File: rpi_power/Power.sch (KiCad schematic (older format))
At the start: 27 parts, among them U1 TPS54625

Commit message: Updated some footprints.
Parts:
- C10, C11: footprint Capacitor_Tantalum_SMD:CP_EIA-3216-10_Kemet-I_Pad1.58x1.35mm_HandSolder -> Capacitors:Tantalum_SMD_3216_KEMET_T491_HandSolder
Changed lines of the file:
@@
 F 0 "C10" H 9568 3146 50  0000 L CNN
 F 1 "22uF/6.3V" H 9568 3055 50  0000 L CNN
-F 2 "Capacitor_Tantalum_SMD:CP_EIA-3216-10_Kemet-I_Pad1.58x1.35mm_HandSolder" H 9488 2950 50  0001 C CNN
+F 2 "Capacitors:Tantalum_SMD_3216_KEMET_T491_HandSolder" H 9488 2950 50  0001 C CNN
 F 3 "~" H 9450 3100 50  0001 C CNN
 F 4 "2321204" H 150 -300 50  0001 C CNN "Farnell"
@@
 F 0 "C11" H 10118 2646 50  0000 L CNN
 F 1 "22uF/6.3V" H 10118 2555 50  0000 L CNN
-F 2 "Capacitor_Tantalum_SMD:CP_EIA-3216-10_Kemet-I_Pad1.58x1.35mm_HandSolder" H 10038 2450 50  0001 C CNN
+F 2 "Capacitors:Tantalum_SMD_3216_KEMET_T491_HandSolder" H 10038 2450 50  0001 C CNN
 F 3 "~" H 10000 2600 50  0001 C CNN
 F 4 "2321204" H 700 -800 50  0001 C CNN "Farnell"

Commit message: Routing done, pending review.
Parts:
- U1: footprint TexasInstruments:HTSSOP-14-PWP -> TexasInstruments:HTSSOP-14-PWP_Handsolder
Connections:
- wire segments 106 -> 92
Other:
- moved on the sheet: C1, C10, C11, C2, C3, C4, C5, C6, C7, C8, C9, D1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

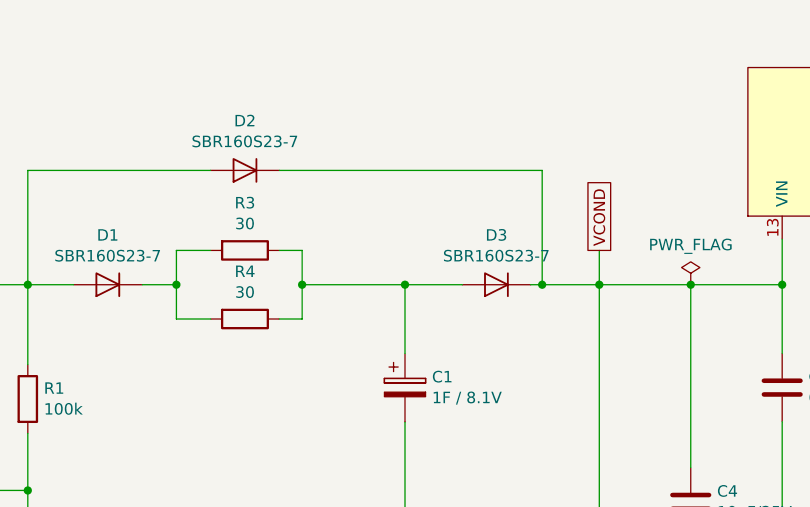
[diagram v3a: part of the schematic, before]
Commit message: Differentiated VCOND and BATT+. Routing done.
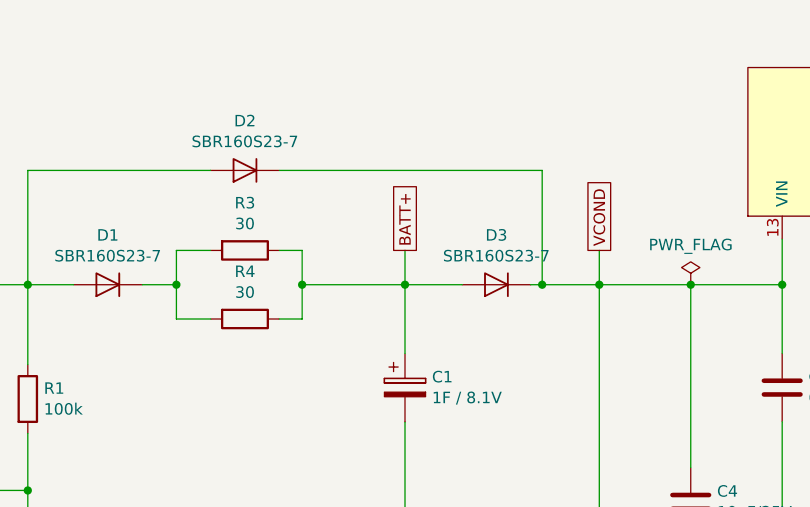
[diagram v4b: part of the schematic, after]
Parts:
- MH1, MH2, MH3, MH4: footprint MountingHole:MountingHole_3.2mm_M3_DIN965 -> Pads:MountingHole_M3-5.8_Pad_Via
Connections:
- net BATT+: now reaches C1.1, D3.2 (A), R3.1, R4.1
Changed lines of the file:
@@
 F 0 "MH1" V 3637 6455 50  0000 C CNN
 F 1 "MountingHole_Pad" V 3546 6455 50  0000 C CNN
-F 2 "MountingHole:MountingHole_3.2mm_M3_DIN965" H 3400 6450 50  0001 C CNN
+F 2 "Pads:MountingHole_M3-5.8_Pad_Via" H 3400 6450 50  0001 C CNN
 F 3 "~" H 3400 6450 50  0001 C CNN
 	1    3400 6450
@@
 Wire Wire Line
 	4750 2350 5150 2350
-$Comp
-L Mechanical:MountingHole_Pad MH2
-U 1 1 5BECA8ED
-P 3400 6900
-F 0 "MH2" V 3637 6905 50  0000 C CNN
-F 1 "MountingHole_Pad" V 3546 6905 50  0000 C CNN
-F 2 "MountingHole:MountingHole_3.2mm_M3_DIN965" H 3400 6900 50  0001 C CNN
-F 3 "~" H 3400 6900 50  0001 C CNN
-	1    3400 6900
-	0    -1   -1   0
-$EndComp
-$Comp
-L Mechanical:MountingHole_Pad MH3
-U 1 1 5BECA939
-P 4300 6450
-F 0 "MH3" V 4537 6455 50  0000 C CNN
-F 1 "MountingHole_Pad" V 4446 6455 50  0000 C CNN
-F 2 "MountingHole:MountingHole_3.2mm_M3_DIN965" H 4300 6450 50  0001 C CNN
-F 3 "~" H 4300 6450 50  0001 C CNN
-	1    4300 6450
-	0    1    1    0
-$EndComp
-$Comp
-L Mechanical:MountingHole_Pad MH4
-U 1 1 5BECA9BB
-P 4300 6900
-F 0 "MH4" V 4537 6905 50  0000 C CNN
-F 1 "MountingHole_Pad" V 4446 6905 50  0000 C CNN
-F 2 "MountingHole:MountingHole_3.2mm_M3_DIN965" H 4300 6900 50  0001 C CNN
-F 3 "~" H 4300 6900 50  0001 C CNN
-	1    4300 6900
-	0    1    1    0
-$EndComp
 Wire Wire Line
 	5150 2350 5550 2350
@@
 Wire Wire Line
 	6650 2150 6650 4250
+$Comp
+L Mechanical:MountingHole_Pad MH2
+U 1 1 5BE34C4E
+P 3400 6900
+F 0 "MH2" V 3637 6905 50  0000 C CNN
+F 1 "MountingHole_Pad" V 3546 6905 50  0000 C CNN
+F 2 "Pads:MountingHole_M3-5.8_Pad_Via" H 3400 6900 50  0001 C CNN
+F 3 "~" H 3400 6900 50  0001 C CNN
+	1    3400 6900
+	0    -1   -1   0
+$EndComp
+$Comp
+L Mechanical:MountingHole_Pad MH3
+U 1 1 5BE34C9A
+P 4300 6450
+F 0 "MH3" V 4537 6455 50  0000 C CNN
+F 1 "MountingHole_Pad" V 4446 6455 50  0000 C CNN
+F 2 "Pads:MountingHole_M3-5.8_Pad_Via" H 4300 6450 50  0001 C CNN
+F 3 "~" H 4300 6450 50  0001 C CNN
+	1    4300 6450
+	0    1    1    0
+$EndComp
+$Comp
+L Mechanical:MountingHole_Pad MH4
+U 1 1 5BE34D2A
+P 4300 6900
+F 0 "MH4" V 4537 6905 50  0000 C CNN
+F 1 "MountingHole_Pad" V 4446 6905 50  0000 C CNN
+F 2 "Pads:MountingHole_M3-5.8_Pad_Via" H 4300 6900 50  0001 C CNN
+F 3 "~" H 4300 6900 50  0001 C CNN
+	1    4300 6900
+	0    1    1    0
+$EndComp
+Wire Wire Line
+	3900 2350 3900 2200
+Text GLabel 3900 2200 1    50   UnSpc ~ 0
+BATT+
 $EndSCHEMATC
